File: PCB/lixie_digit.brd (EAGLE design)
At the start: 62.3 x 38 mm, 23 parts

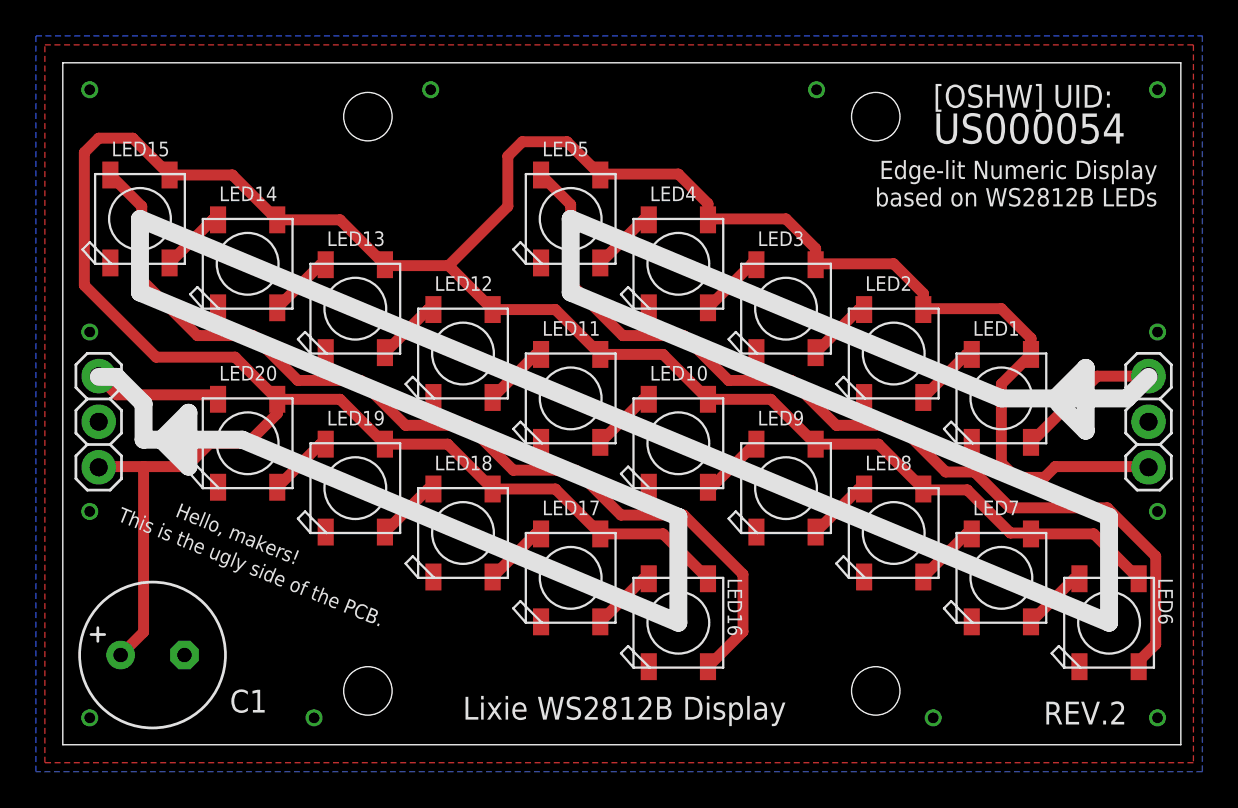
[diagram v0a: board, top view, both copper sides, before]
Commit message: Switched pin order to standard
Power/ground/data order changed to power/data/ground.
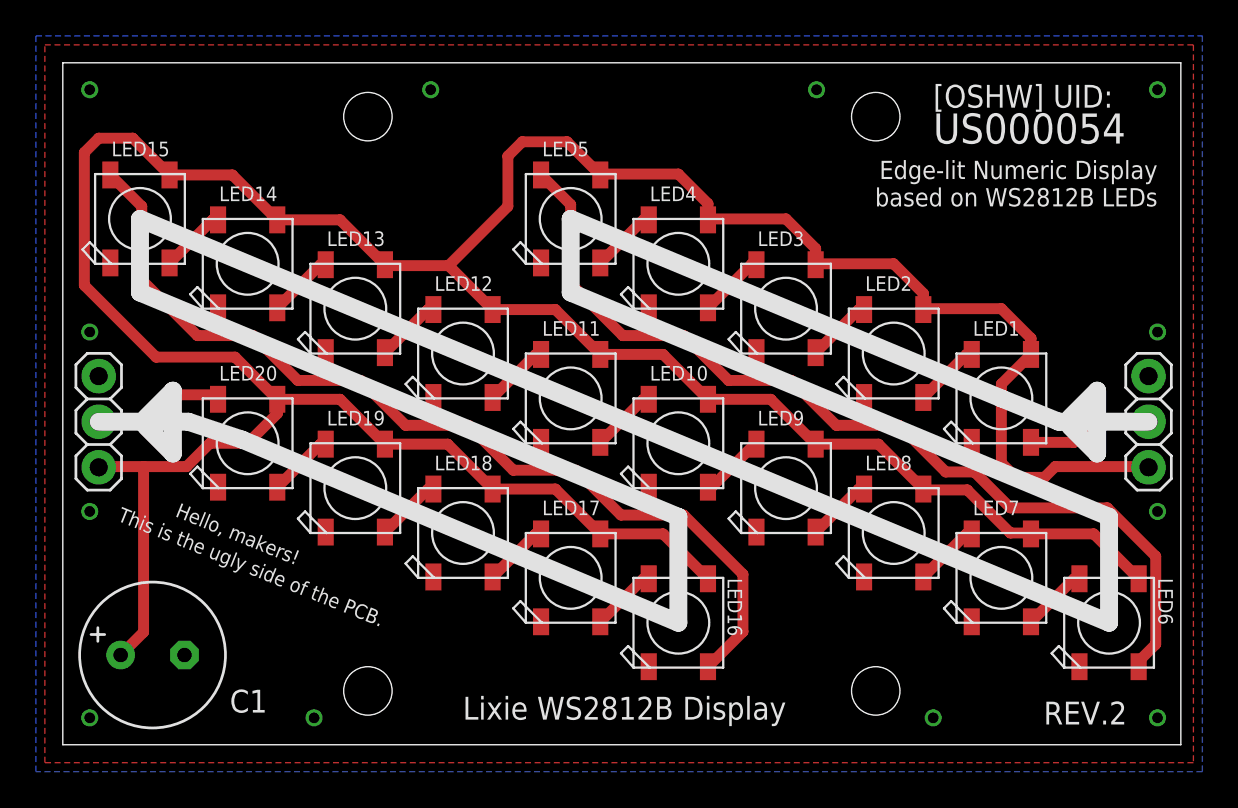
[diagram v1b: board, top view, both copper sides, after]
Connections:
- net N$20 renamed 5V
- removed net N$23: JP1.1, LED1.4-DIN
- removed net N$24: JP2.3, LED20.2-DOUT
- new net DIN: JP1.2, LED1.4-DIN
- new net DOUT: JP2.2, LED20.2-DOUT
- net GND: now also JP1.1, JP2.3; no longer JP1.2, JP2.2
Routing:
- net N$23: track 8.08 -> 0.00 mm
- net N$24: track 7.47 -> 0.00 mm
- net DOUT: track 0.00 -> 7.33 mm
- net DIN: track 0.00 -> 7.03 mm
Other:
- board text added: "Last Updated: December 18th, 2016"
- board text removed: "Last Updated: December 16th, 2016"
